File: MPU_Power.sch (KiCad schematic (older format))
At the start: 42 parts, among them U1 STM32MP151AAB3

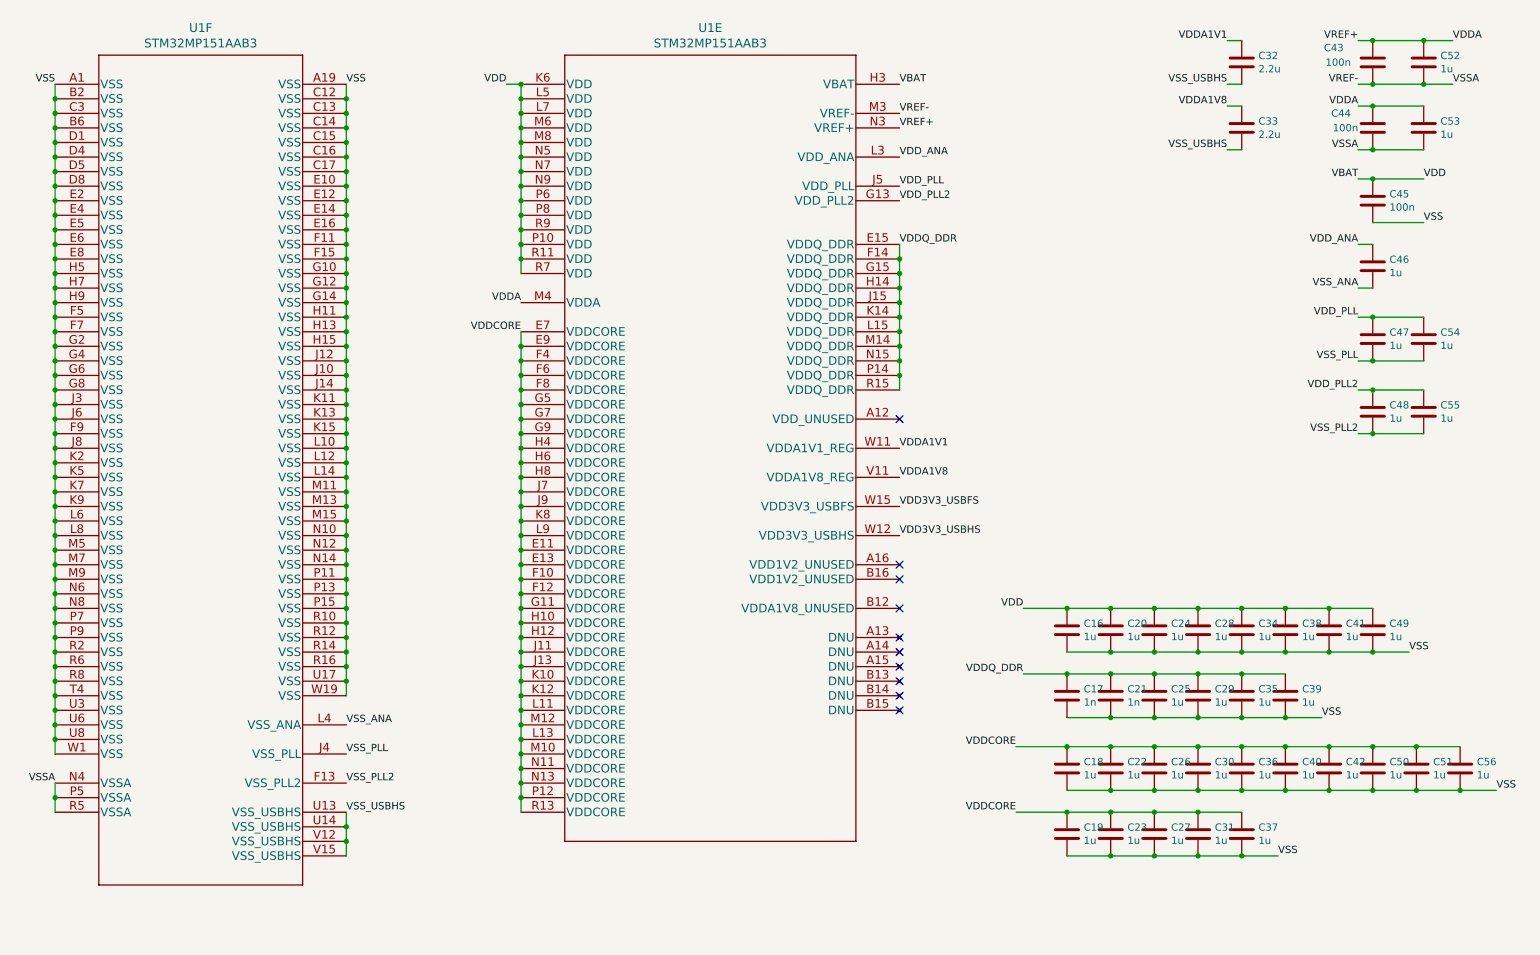
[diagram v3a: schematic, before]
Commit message: Add DC barrel connector for alternate power supply
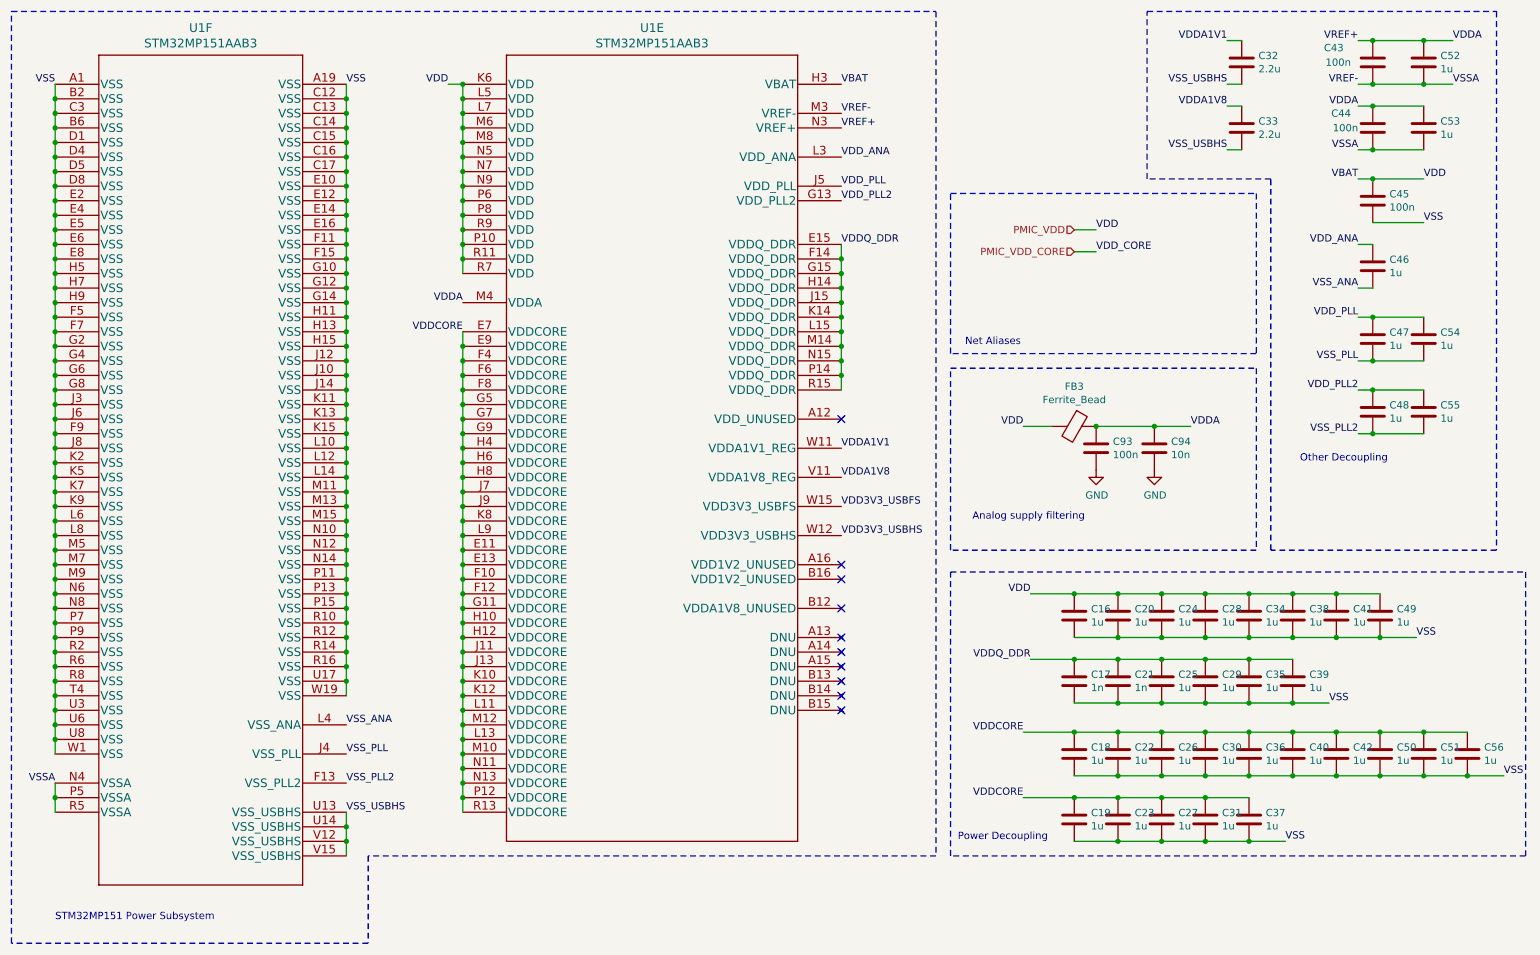
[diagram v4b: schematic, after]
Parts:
- added C93: 100n, symbol Device:C
- added C94: 10n, symbol Device:C
- added FB3: Ferrite_Bead, symbol Device:Ferrite_Bead
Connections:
- net VDDA: now also C93.1, C94.1, FB3.1
- net VBAT renamed PMIC_VDD
- net PMIC_VDD: now also FB3.2
- new net GND: C93.2, C94.2
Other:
- note added: "Analog supply filtering"
- note added: "Net Aliases"
- note added: "Other Decoupling"
- note added: "Power Decoupling"
- note added: "STM32MP151 Power Subsystem"
- moved on the sheet: C16, C17, C18, C19, C20, C21, C22, C23, C24, C25, C26, C27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

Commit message: Start crossing off ERC. Add generated BOM
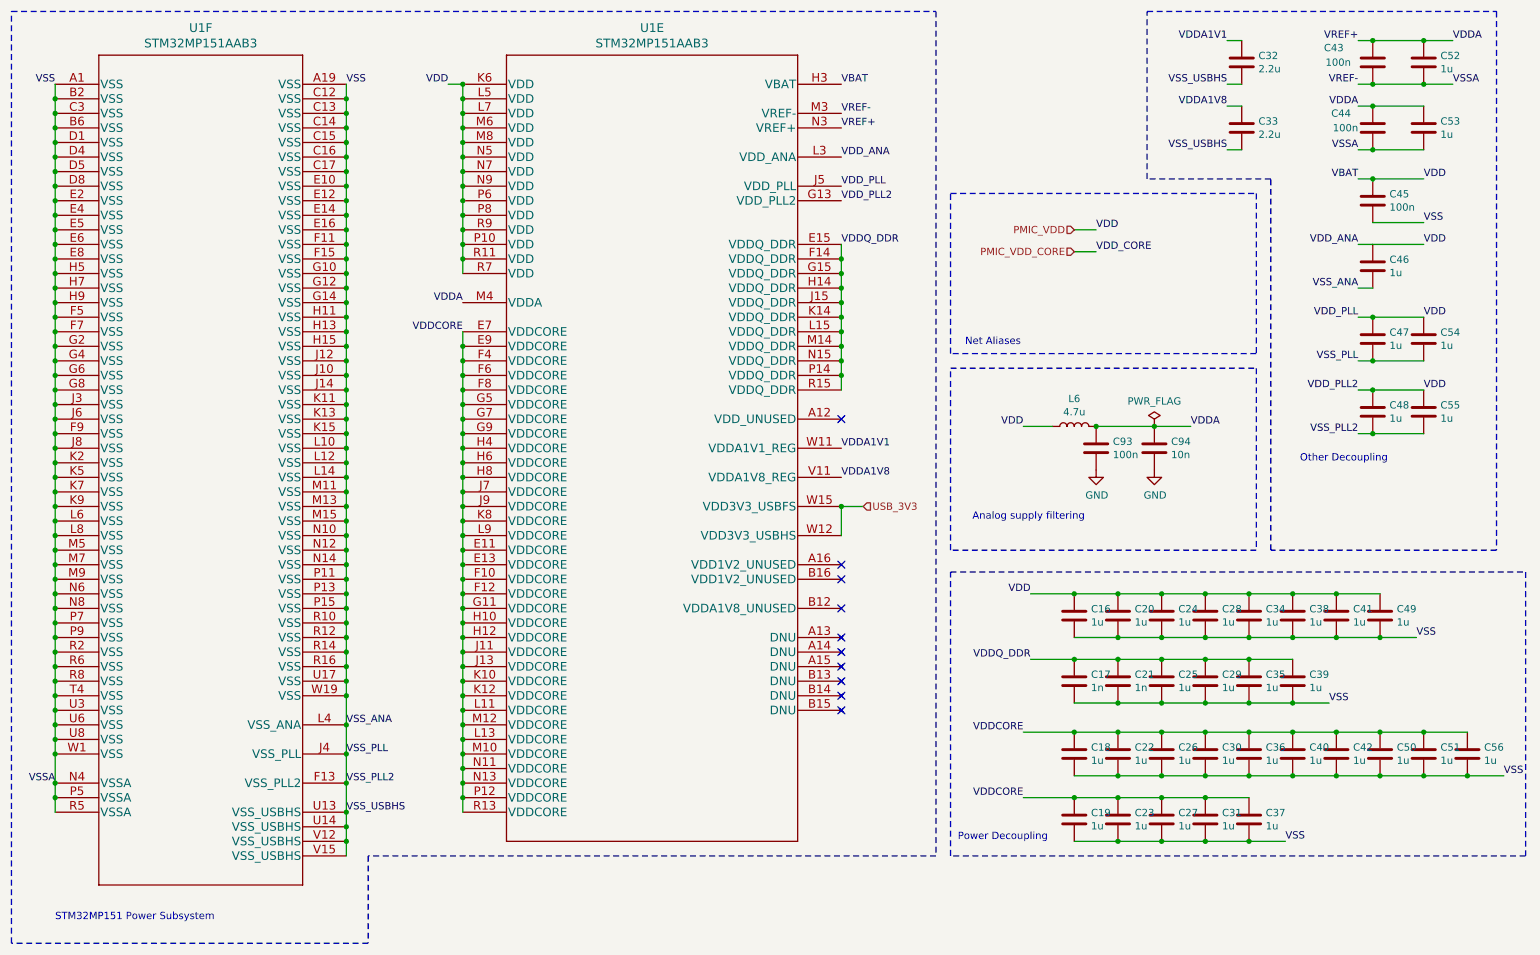
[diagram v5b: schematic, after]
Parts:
- removed FB3: Ferrite_Bead, symbol Device:Ferrite_Bead
- added L6: 4.7u, symbol Device:L
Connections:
- net VDD3V3_USBHS is gone; now on net USB_3V3: U1.W12 (VDD3V3_USBHS)
- net VDD_ANA is gone; now on net PMIC_VDD: C46.1, U1.L3 (VDD_ANA)
- net VDD_PLL is gone; now on net PMIC_VDD: C47.1, C54.1, U1.J5 (VDD_PLL)
- net VDD_PLL2 is gone; now on net PMIC_VDD: C48.1, C55.1, U1.G13 (VDD_PLL2)
- net VSS is gone; now on net VREF-: C16.2, C17.2, C18.2, C19.2, C20.2, C21.2, C22.2, C23.2, C24.2, C25.2, C26.2, C27.2, C28.2, C29.2, C30.2, C31.2, C34.2, C35.2, C36.2, C37.2, C38.2, C39.2, C40.2, C41.2, C42.2, C45.2, C49.2, C50.2, C51.2, C56.2, U1.A1 (VSS), U1.A19 (VSS), U1.B2 (VSS), U1.B6 (VSS), U1.C12 (VSS), U1.C13 (VSS), U1.C14 (VSS), U1.C15 (VSS), U1.C16 (VSS), U1.C17 (VSS), U1.C3 (VSS), U1.D1 (VSS), U1.D4 (VSS), U1.D5 (VSS), U1.D8 (VSS), U1.E10 (VSS), U1.E12 (VSS), U1.E14 (VSS), U1.E16 (VSS), U1.E2 (VSS), U1.E4 (VSS), U1.E5 (VSS), U1.E6 (VSS), U1.E8 (VSS), U1.F11 (VSS), U1.F15 (VSS), U1.F5 (VSS), U1.F7 (VSS), U1.F9 (VSS), U1.G10 (VSS), U1.G12 (VSS), U1.G14 (VSS), U1.G2 (VSS), U1.G4 (VSS), U1.G6 (VSS), U1.G8 (VSS), U1.H11 (VSS), U1.H13 (VSS), U1.H15 (VSS), U1.H5 (VSS), U1.H7 (VSS), U1.H9 (VSS), U1.J10 (VSS), U1.J12 (VSS), U1.J14 (VSS), U1.J3 (VSS), U1.J6 (VSS), U1.J8 (VSS), U1.K11 (VSS), U1.K13 (VSS), U1.K15 (VSS), U1.K2 (VSS), U1.K5 (VSS), U1.K7 (VSS), U1.K9 (VSS), U1.L10 (VSS), U1.L12 (VSS), U1.L14 (VSS), U1.L6 (VSS), U1.L8 (VSS), U1.M11 (VSS), U1.M13 (VSS), U1.M15 (VSS), U1.M5 (VSS), U1.M7 (VSS), U1.M9 (VSS), U1.N10 (VSS), U1.N12 (VSS), U1.N14 (VSS), U1.N6 (VSS), U1.N8 (VSS), U1.P11 (VSS), U1.P13 (VSS), U1.P15 (VSS), U1.P7 (VSS), U1.P9 (VSS), U1.R10 (VSS), U1.R12 (VSS), U1.R14 (VSS), U1.R16 (VSS), U1.R2 (VSS), U1.R6 (VSS), U1.R8 (VSS), U1.T4 (VSS), U1.U17 (VSS), U1.U3 (VSS), U1.U6 (VSS), U1.U8 (VSS), U1.W1 (VSS), U1.W19 (VSS)
- net VSS_ANA is gone; now on net VREF-: C46.2, U1.L4 (VSS_ANA)
- net VSS_PLL is gone; now on net VREF-: C47.2, C54.2, U1.J4 (VSS_PLL)
- net VSS_PLL2 is gone; now on net VREF-: C48.2, C55.2, U1.F13 (VSS_PLL2)
- net VSS_USBHS is gone; now on net VREF-: C32.2, C33.2, U1.U13 (VSS_USBHS), U1.U14 (VSS_USBHS), U1.V12 (VSS_USBHS), U1.V15 (VSS_USBHS)
- net PMIC_VDD: now also L6.1
- net VDDA: now also L6.2
- net VDD3V3_USBFS renamed USB_3V3
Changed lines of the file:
@@
-	1    0    0    -1
-$EndComp
-$Comp
-L LinuxBoard:STM32MP151AAB3 U?
-U 5 1 60484467
-P 3850 1100
-AR Path="/60172A77/60484467" Ref="U?"  Part="5"
-AR Path="/601728E9/60484467" Ref="U1"  Part="5"
-F 0 "U1" H 5150 1487 60  0000 C CNN
-F 1 "STM32MP151AAB3" H 5150 1381 60  0000 C CNN
-F 2 "LinuxBoard:STM32MP151AAB3" H 4850 1340 60  0001 C CNN
-F 3 "" H 3850 1100 60  0000 C CNN
-	5    3850 1100
 	1    0    0    -1
 $EndComp
@@
 Wire Wire Line
 	3050 6300 3050 6400
-Wire Wire Line
-	3850 2800 3850 2900
-Connection ~ 3850 2900
-Wire Wire Line
-	3850 2900 3850 3000
-Connection ~ 3850 3000
-Wire Wire Line
-	3850 3000 3850 3100
-Connection ~ 3850 3100
-Wire Wire Line
-	3850 3100 3850 3200
-Connection ~ 3850 3200
-Wire Wire Line
-	3850 3200 3850 3300
-Connection ~ 3850 3300
-Wire Wire Line
-	3850 3300 3850 3400
-Connection ~ 3850 3400
-Wire Wire Line
-	3850 3400 3850 3500
-Connection ~ 3850 3500
-Wire Wire Line
-	3850 3500 3850 3600
-Connection ~ 3850 3600
-Wire Wire Line
-	3850 3600 3850 3700
-Connection ~ 3850 3700
-Wire Wire Line
-	3850 3700 3850 3800
-Connection ~ 3850 3800
-Wire Wire Line
-	3850 3800 3850 3900
-Connection ~ 3850 3900
-Wire Wire Line
-	3850 3900 3850 4000
-Connection ~ 3850 4000
-Wire Wire Line
-	3850 4000 3850 4100
-Connection ~ 3850 4100
-Wire Wire Line
-	3850 4100 3850 4200
-Connection ~ 3850 4200
-Wire Wire Line
-	3850 4200 3850 4300
-Connection ~ 3850 4300
-Wire Wire Line
-	3850 4300 3850 4400
-Connection ~ 3850 4400
-Wire Wire Line
-	3850 4400 3850 4500
-Connection ~ 3850 4500
-Wire Wire Line
-	3850 4500 3850 4600
-Connection ~ 3850 4600
-Wire Wire Line
-	3850 4600 3850 4700
-Connection ~ 3850 4700
-Wire Wire Line
-	3850 4700 3850 4800
-Connection ~ 3850 4800
-Wire Wire Line
-	3850 4800 3850 4900
-Connection ~ 3850 4900
-Wire Wire Line
-	3850 4900 3850 5000
-Connection ~ 3850 5000
-Wire Wire Line
-	3850 5000 3850 5100
-Connection ~ 3850 5100
-Wire Wire Line
-	3850 5100 3850 5200
-Connection ~ 3850 5200
-Wire Wire Line
-	3850 5200 3850 5300
-Connection ~ 3850 5300
-Wire Wire Line
-	3850 5300 3850 5400
-Connection ~ 3850 5400
-Wire Wire Line
-	3850 5400 3850 5500
-Connection ~ 3850 5500
-Wire Wire Line
-	3850 5500 3850 5600
-Connection ~ 3850 5600
-Wire Wire Line
-	3850 5600 3850 5700
-Connection ~ 3850 5700
-Wire Wire Line
-	3850 5700 3850 5800
-Connection ~ 3850 5800
-Wire Wire Line
-	3850 5800 3850 5900
-Connection ~ 3850 5900
-Wire Wire Line
-	3850 5900 3850 6000
-Connection ~ 3850 6000
-Wire Wire Line
-	3850 6000 3850 6100
-Wire Wire Line
-	3850 2400 3850 2300
-Connection ~ 3850 1200
-Wire Wire Line
-	3850 1200 3850 1100
-Connection ~ 3850 1300
-Wire Wire Line
-	3850 1300 3850 1200
-Connection ~ 3850 1400
-Wire Wire Line
-	3850 1400 3850 1300
-Connection ~ 3850 1500
-Wire Wire Line
-	3850 1500 3850 1400
-Connection ~ 3850 1600
-Wire Wire Line
-	3850 1600 3850 1500
-Connection ~ 3850 1700
-Wire Wire Line
-	3850 1700 3850 1600
-Connection ~ 3850 1800
-Wire Wire Line
-	3850 1800 3850 1700
-Connection ~ 3850 1900
-Wire Wire Line
-	3850 1900 3850 1800
-Connection ~ 3850 2000
-Wire Wire Line
-	3850 2000 3850 1900
-Connection ~ 3850 2100
-Wire Wire Line
-	3850 2100 3850 2000
-Connection ~ 3850 2200
-Wire Wire Line
-	3850 2200 3850 2100
-Connection ~ 3850 2300
-Wire Wire Line
-	3850 2300 3850 2200
-Wire Wire Line
-	6450 2200 6450 2300
-Connection ~ 6450 2300
-Wire Wire Line
-	6450 2300 6450 2400
-Connection ~ 6450 2400
-Wire Wire Line
-	6450 2400 6450 2500
-Connection ~ 6450 2500
-Wire Wire Line
-	6450 2500 6450 2600
-Connection ~ 6450 2600
-Wire Wire Line
-	6450 2600 6450 2700
-Connection ~ 6450 2700
-Wire Wire Line
-	6450 2700 6450 2800
-Connection ~ 6450 2800
-Wire Wire Line
-	6450 2800 6450 2900
-Connection ~ 6450 2900
-Wire Wire Line
-	6450 2900 6450 3000
-Connection ~ 6450 3000
-Wire Wire Line
-	6450 3000 6450 3100
-Connection ~ 6450 3100
-Wire Wire Line
-	6450 3100 6450 3200
 Text Label 3750 1100 2    50   ~ 0
 VDD
 Wire Wire Line
 	3750 1100 3850 1100
-Connection ~ 3850 1100
 NoConn ~ 6450 5400
 NoConn ~ 6450 5300
@@
 	10100 3000 10450 3000
 Connection ~ 10100 3000
-Wire Wire Line
-	10100 2700 10450 2700
 Connection ~ 10100 2700
 $Comp
@@
 Text Label 6450 3800 0    50   ~ 0
 VDDA1V8
-Text Label 6450 4000 0    50   ~ 0
-VDD3V3_USBFS
-Text Label 6450 4200 0    50   ~ 0
-VDD3V3_USBHS
 Text Label 9100 800  2    50   ~ 0
 VDDA1V1
@@
 Net Aliases
 $Comp
-L Device:Ferrite_Bead FB?
-U 1 1 61A9B365
-P 8050 3450
-AR Path="/60172AD8/61A9B365" Ref="FB?"  Part="1"
-AR Path="/601728E9/61A9B365" Ref="FB3"  Part="1"
-F 0 "FB3" V 7776 3450 50  0000 C CNN
-F 1 "Ferrite_Bead" V 7867 3450 50  0000 C CNN
-F 2 "" V 7980 3450 50  0001 C CNN
-F 3 "~" H 8050 3450 50  0001 C CNN
-	1    8050 3450
-	0    1    1    0
-$EndComp
-$Comp
 L Device:C C?
 U 1 1 61A9B36B
@@
 Wire Wire Line
 	8200 3450 8600 3450
-Connection ~ 8200 3450
 Wire Wire Line
 	7700 3450 7900 3450
@@
 Wire Notes Line
 	9300 2950 7200 2950
+Wire Wire Line
+	3050 5900 3050 5700
+Wire Wire Line
+	3050 5700 3050 5500
+Connection ~ 3050 5700
+Wire Wire Line
+	1050 5900 1050 5700
+Connection ~ 1050 5900
+Connection ~ 1050 5700
+Wire Wire Line
+	3050 5900 3050 6100
+Connection ~ 3050 5900
+Connection ~ 3050 6100
+Wire Wire Line
+	3050 5500 3050 5300
+Connection ~ 3050 5500
+Connection ~ 3050 5300
+$Comp
+L power:PWR_FLAG #FLG0101
+U 1 1 609CDD62
+P 8600 3450
+F 0 "#FLG0101" H 8600 3525 50  0001 C CNN
+F 1 "PWR_FLAG" H 8600 3623 50  0000 C CNN
+F 2 "" H 8600 3450 50  0001 C CNN
+F 3 "~" H 8600 3450 50  0001 C CNN
+	1    8600 3450
+	1    0    0    -1
+$EndComp
+$Comp
+L Device:L L6
+U 1 1 609E388D
+P 8050 3450
+F 0 "L6" V 8240 3450 50  0000 C CNN
+F 1 "4.7u" V 8149 3450 50  0000 C CNN
+F 2 "" H 8050 3450 50  0001 C CNN
+F 3 "~" H 8050 3450 50  0001 C CNN
+	1    8050 3450
+	0    -1   -1   0
+$EndComp
+Connection ~ 8200 3450
+Connection ~ 3850 2100
+Wire Wire Line
+	3850 2400 3850 2300
+Connection ~ 3850 2300
+Wire Wire Line
+	3850 2100 3850 2000
+Connection ~ 3850 2000
+Wire Wire Line
+	3850 2000 3850 1900
+Connection ~ 3850 1900
+Wire Wire Line
+	6450 3100 6450 3200
+Connection ~ 6450 3100
+Wire Wire Line
+	3850 6000 3850 6100
+Connection ~ 3850 6000
+Wire Wire Line
+	3850 2300 3850 2200
+Wire Wire Line
+	3850 2200 3850 2100
+Connection ~ 3850 2200
+Wire Wire Line
+	3850 1900 3850 1800
+Connection ~ 3850 1800
+Wire Wire Line
+	3850 1800 3850 1700
+Connection ~ 3850 1700
+Wire Wire Line
+	3850 1700 3850 1600
+Connection ~ 3850 1600
+Wire Wire Line
+	6450 3000 6450 3100
+Connection ~ 6450 3000
+Wire Wire Line
+	3850 5900 3850 6000
+Connection ~ 3850 5900
+Wire Wire Line
+	3850 5800 3850 5900
+Connection ~ 3850 5800
+Wire Wire Line
+	3850 1600 3850 1500
+Connection ~ 3850 1500
+Wire Wire Line
+	3850 1500 3850 1400
+Connection ~ 3850 1400
+Wire Wire Line
+	6450 2900 6450 3000
+Connection ~ 6450 2900
+Connection ~ 3850 5500
+Wire Wire Line
+	3850 5700 3850 5800
+Connection ~ 3850 5700
+Connection ~ 3850 4200
+Wire Wire Line
+	3850 1400 3850 1300
+Connection ~ 3850 1300
+Wire Wire Line
+	3850 1300 3850 1200
+Wire Wire Line
+	3850 1200 3850 1100
+Connection ~ 3850 1200
+Wire Wire Line
+	6450 2800 6450 2900
+Connection ~ 6450 2800
+Wire Wire Line
+	3850 5600 3850 5700
+Wire Wire Line
+	3850 5500 3850 5600
+Connection ~ 3850 5600
+Wire Wire Line
+	3850 5400 3850 5500
+Connection ~ 3850 5400
+Wire Wire Line
+	3850 4100 3850 4200
+Connection ~ 3850 4100
+Connection ~ 3850 1100
+Wire Wire Line
+	6450 2700 6450 2800
+Connection ~ 6450 2700
+Wire Wire Line
+	3850 5300 3850 5400
+Connection ~ 3850 5300
+Wire Wire Line
+	3850 5200 3850 5300
+Connection ~ 3850 5200
+Wire Wire Line
+	3850 4000 3850 4100
+Connection ~ 3850 4000
+Wire Wire Line
+	3850 3900 3850 4000
+Connection ~ 3850 3900
+Wire Wire Line
+	6450 2600 6450 2700
+Connection ~ 6450 2600
+Wire Wire Line
+	3850 5100 3850 5200
+Connection ~ 3850 5100
+Wire Wire Line
+	3850 5000 3850 5100
+Connection ~ 3850 5000
+Wire Wire Line
+	3850 3800 3850 3900
+Connection ~ 3850 3800
+Wire Wire Line
+	3850 3700 3850 3800
+Connection ~ 3850 3700
+Wire Wire Line
+	3850 3600 3850 3700
+Connection ~ 3850 3600
+Wire Wire Line
+	6450 2500 6450 2600
+Connection ~ 6450 2500
+Wire Wire Line
+	3850 4900 3850 5000
+Connection ~ 3850 4900
+Wire Wire Line
+	3850 4800 3850 4900
+Connection ~ 3850 4800
+Wire Wire Line
+	3850 3500 3850 3600
+Connection ~ 3850 3500
+Wire Wire Line
+	3850 3400 3850 3500
+Connection ~ 3850 3400
+Wire Wire Line
+	3850 3300 3850 3400
+Connection ~ 3850 3300
+Wire Wire Line
+	6450 2400 6450 2500
+Connection ~ 6450 2400
+Wire Wire Line
+	3850 4700 3850 4800
+Connection ~ 3850 4700
+Wire Wire Line
+	3850 3200 3850 3300
+Connection ~ 3850 3200
+Wire Wire Line
+	3850 3100 3850 3200
+Connection ~ 3850 3100
+Wire Wire Line
+	3850 3000 3850 3100
+Connection ~ 3850 3000
+Wire Wire Line
+	6450 2300 6450 2400
+Wire Wire Line
+	6450 2200 6450 2300
+Connection ~ 6450 2300
+Wire Wire Line
+	3850 4600 3850 4700
+Connection ~ 3850 4600
+Wire Wire Line
+	3850 4500 3850 4600
+Connection ~ 3850 4500
+Wire Wire Line
+	3850 2900 3850 3000
+Wire Wire Line
+	3850 2800 3850 2900
+Connection ~ 3850 2900
+Wire Wire Line
+	3850 4400 3850 4500
+Connection ~ 3850 4400
+Wire Wire Line
+	3850 4300 3850 4400
+Wire Wire Line
+	3850 4200 3850 4300
+Connection ~ 3850 4300
+$Comp
+L LinuxBoard:STM32MP151AAB3 U?
+U 5 1 60484467
+P 3850 1100
+AR Path="/60172A77/60484467" Ref="U?"  Part="5"
+AR Path="/601728E9/60484467" Ref="U1"  Part="5"
+F 0 "U1" H 5150 1487 60  0000 C CNN
+F 1 "STM32MP151AAB3" H 5150 1381 60  0000 C CNN
+F 2 "LinuxBoard:STM32MP151AAB3" H 4850 1340 60  0001 C CNN
+F 3 "" H 3850 1100 60  0000 C CNN
+	5    3850 1100
+	1    0    0    -1
+$EndComp
+Text Label 10450 2200 0    50   ~ 0
+VDD
+Wire Wire Line
+	10100 2200 10450 2200
+Wire Wire Line
+	10100 2700 10450 2700
+Text Label 10450 2700 0    50   ~ 0
+VDD
+Text Label 10450 3200 0    50   ~ 0
+VDD
+Wire Wire Line
+	6450 4000 6450 4200
+Text HLabel 6600 4000 2    50   Input ~ 0
+USB_3V3
+Wire Wire Line
+	6600 4000 6450 4000
+Connection ~ 6450 4000
 $EndSCHEMATC

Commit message: Complete schematic rough draft
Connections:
- net VREF- is gone; now on net GND: C16.2, C17.2, C18.2, C19.2, C20.2, C21.2, C22.2, C23.2, C24.2, C25.2, C26.2, C27.2, C28.2, C29.2, C30.2, C31.2, C32.2, C33.2, C34.2, C35.2, C36.2, C37.2, C38.2, C39.2, C40.2, C41.2, C42.2, C43.1, C44.1, C45.2, C46.2, C47.2, C48.2, C49.2, C50.2, C51.2, C52.2, C53.2, C54.2, C55.2, C56.2, U1.A1 (VSS), U1.A19 (VSS), U1.B2 (VSS), U1.B6 (VSS), U1.C12 (VSS), U1.C13 (VSS), U1.C14 (VSS), U1.C15 (VSS), U1.C16 (VSS), U1.C17 (VSS), U1.C3 (VSS), U1.D1 (VSS), U1.D4 (VSS), U1.D5 (VSS), U1.D8 (VSS), U1.E10 (VSS), U1.E12 (VSS), U1.E14 (VSS), U1.E16 (VSS), U1.E2 (VSS), U1.E4 (VSS), U1.E5 (VSS), U1.E6 (VSS), U1.E8 (VSS), U1.F11 (VSS), U1.F13 (VSS_PLL2), U1.F15 (VSS), U1.F5 (VSS), U1.F7 (VSS), U1.F9 (VSS), U1.G10 (VSS), U1.G12 (VSS), U1.G14 (VSS), U1.G2 (VSS), U1.G4 (VSS), U1.G6 (VSS), U1.G8 (VSS), U1.H11 (VSS), U1.H13 (VSS), U1.H15 (VSS), U1.H5 (VSS), U1.H7 (VSS), U1.H9 (VSS), U1.J10 (VSS), U1.J12 (VSS), U1.J14 (VSS), U1.J3 (VSS), U1.J4 (VSS_PLL), U1.J6 (VSS), U1.J8 (VSS), U1.K11 (VSS), U1.K13 (VSS), U1.K15 (VSS), U1.K2 (VSS), U1.K5 (VSS), U1.K7 (VSS), U1.K9 (VSS), U1.L10 (VSS), U1.L12 (VSS), U1.L14 (VSS), U1.L4 (VSS_ANA), U1.L6 (VSS), U1.L8 (VSS), U1.M11 (VSS), U1.M13 (VSS), U1.M15 (VSS), U1.M3 (VREF-), U1.M5 (VSS), U1.M7 (VSS), U1.M9 (VSS), U1.N10 (VSS), U1.N12 (VSS), U1.N14 (VSS), U1.N4 (VSSA), U1.N6 (VSS), U1.N8 (VSS), U1.P11 (VSS), U1.P13 (VSS), U1.P15 (VSS), U1.P5 (VSSA), U1.P7 (VSS), U1.P9 (VSS), U1.R10 (VSS), U1.R12 (VSS), U1.R14 (VSS), U1.R16 (VSS), U1.R2 (VSS), U1.R5 (VSSA), U1.R6 (VSS), U1.R8 (VSS), U1.T4 (VSS), U1.U13 (VSS_USBHS), U1.U14 (VSS_USBHS), U1.U17 (VSS), U1.U3 (VSS), U1.U6 (VSS), U1.U8 (VSS), U1.V12 (VSS_USBHS), U1.V15 (VSS_USBHS), U1.W1 (VSS), U1.W19 (VSS)
- net PMIC_VDD_CORE: now also U1.E11 (VDDCORE), U1.E13 (VDDCORE), U1.E7 (VDDCORE), U1.E9 (VDDCORE), U1.F10 (VDDCORE), U1.F12 (VDDCORE), U1.F4 (VDDCORE), U1.F6 (VDDCORE), U1.F8 (VDDCORE), U1.G11 (VDDCORE), U1.G5 (VDDCORE), U1.G7 (VDDCORE), U1.G9 (VDDCORE), U1.H10 (VDDCORE), U1.H12 (VDDCORE), U1.H4 (VDDCORE), U1.H6 (VDDCORE), U1.H8 (VDDCORE), U1.J11 (VDDCORE), U1.J13 (VDDCORE), U1.J7 (VDDCORE), U1.J9 (VDDCORE), U1.K10 (VDDCORE), U1.K12 (VDDCORE), U1.K8 (VDDCORE), U1.L11 (VDDCORE), U1.L13 (VDDCORE), U1.L9 (VDDCORE), U1.M10 (VDDCORE), U1.M12 (VDDCORE), U1.N11 (VDDCORE), U1.N13 (VDDCORE), U1.P12 (VDDCORE), U1.R13 (VDDCORE)
- net VDDCORE: no longer U1.E11 (VDDCORE), U1.E13 (VDDCORE), U1.E7 (VDDCORE), U1.E9 (VDDCORE), U1.F10 (VDDCORE), U1.F12 (VDDCORE), U1.F4 (VDDCORE), U1.F6 (VDDCORE), U1.F8 (VDDCORE), U1.G11 (VDDCORE), U1.G5 (VDDCORE), U1.G7 (VDDCORE), U1.G9 (VDDCORE), U1.H10 (VDDCORE), U1.H12 (VDDCORE), U1.H4 (VDDCORE), U1.H6 (VDDCORE), U1.H8 (VDDCORE), U1.J11 (VDDCORE), U1.J13 (VDDCORE), U1.J7 (VDDCORE), U1.J9 (VDDCORE), U1.K10 (VDDCORE), U1.K12 (VDDCORE), U1.K8 (VDDCORE), U1.L11 (VDDCORE), U1.L13 (VDDCORE), U1.L9 (VDDCORE), U1.M10 (VDDCORE), U1.M12 (VDDCORE), U1.N11 (VDDCORE), U1.N13 (VDDCORE), U1.P12 (VDDCORE), U1.R13 (VDDCORE)
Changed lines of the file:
@@
 	10450 2050 10100 2050
 Text Label 3850 2800 2    50   ~ 0
-VDDCORE
+VDD_CORE
 Text Label 7700 5550 2    50   ~ 0
 VDDCORE
@@
 Text Label 9500 6300 0    50   ~ 0
 VSS
-Text Label 6450 2200 0    50   ~ 0
-VDDQ_DDR
 Text Label 7750 5050 2    50   ~ 0
 VDDQ_DDR
@@
 Connection ~ 8950 4900
 Connection ~ 10150 4900
-Text Label 6450 3600 0    50   ~ 0
-VDDA1V1
-Text Label 6450 3800 0    50   ~ 0
-VDDA1V8
 Text Label 9100 800  2    50   ~ 0
 VDDA1V1
@@
 Text Label 8200 2250 0    50   ~ 0
 VDD_CORE
-Wire Wire Line
-	8200 2250 8050 2250
 Text Notes 7300 2900 0    50   ~ 0
 Net Aliases
@@
 	6600 4000 6450 4000
 Connection ~ 6450 4000
+Text HLabel 6550 2200 2    50   Input ~ 0
+VDDQ_DDR
+Wire Wire Line
+	6550 2200 6450 2200
+Connection ~ 6450 2200
+Text Label 8200 2400 0    50   ~ 0
+VSS
+$Comp
+L power:GND #PWR0101
+U 1 1 6120E799
+P 8100 2450
+F 0 "#PWR0101" H 8100 2200 50  0001 C CNN
+F 1 "GND" H 8105 2277 50  0000 C CNN
+F 2 "" H 8100 2450 50  0001 C CNN
+F 3 "" H 8100 2450 50  0001 C CNN
+	1    8100 2450
+	1    0    0    -1
+$EndComp
+Wire Wire Line
+	8100 2450 8100 2400
+Wire Wire Line
+	8100 2400 8200 2400
+Wire Wire Line
+	8200 2250 8050 2250
+Text HLabel 6450 3600 2    50   Input ~ 0
+VDDA1V1
+Text HLabel 6450 3800 2    50   Input ~ 0
+VDDA1V8
 $EndSCHEMATC

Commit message: Update footprints
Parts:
- C16, C17, C18, C19, C20, C21, C22, C23, C24, C25, C26, C27, C28, C29, C30, C31, C32, C33, C34, C35, C36, C37, C38, C39, C40, C41, C42, C43, C44, C45, C46, C47, C48, C49, C50, C51, C52, C53, C54, C55, C56, C93, C94: footprint (none) -> Capacitor_SMD:C_0603_1608Metric
- L6: footprint (none) -> Inductor_SMD:L_0603_1608Metric
